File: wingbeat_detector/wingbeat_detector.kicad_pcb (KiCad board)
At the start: 2 copper layers, 36 x 18 mm, 9 parts, among them J1 USB_C_10137062-00021LF, J2 CONN_UMC_JACK_SMD, U1 UAF42_SMA, U2 MAX865EUA+

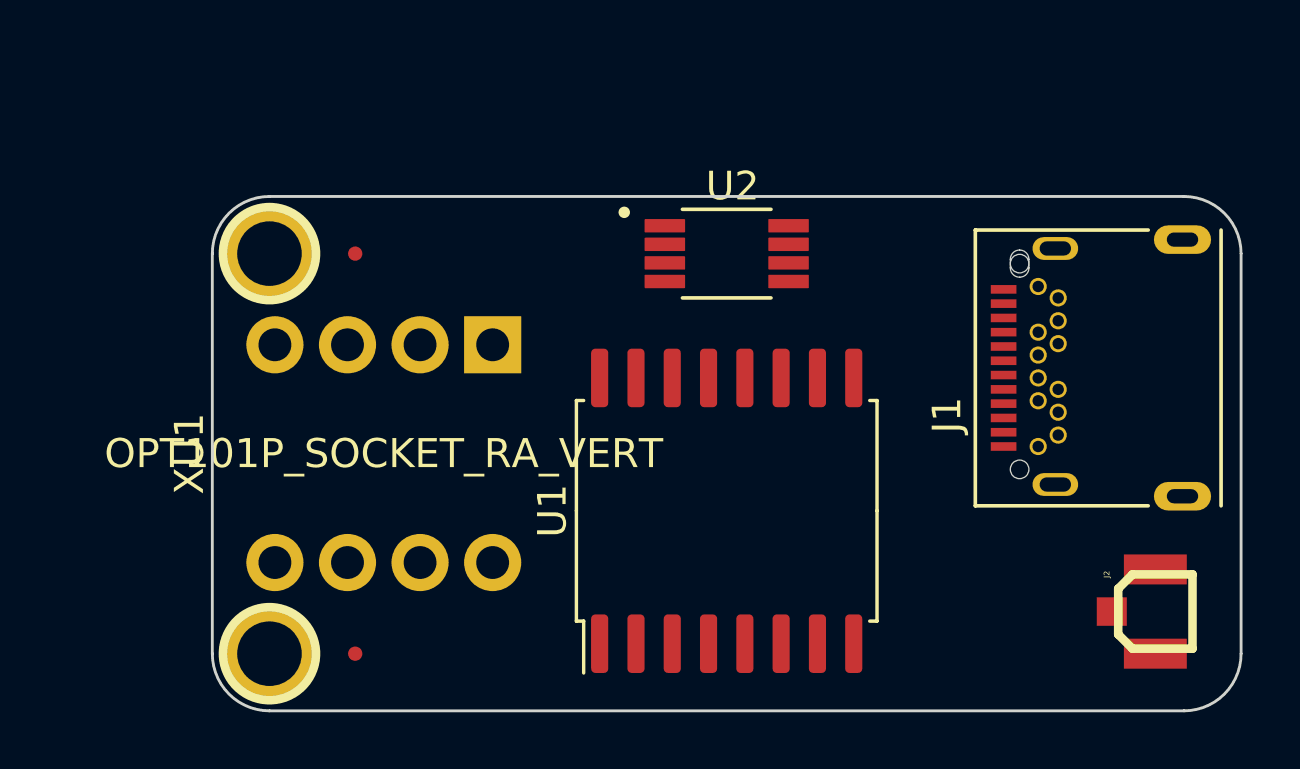
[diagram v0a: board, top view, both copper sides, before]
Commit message: Remove OPT101 and replace
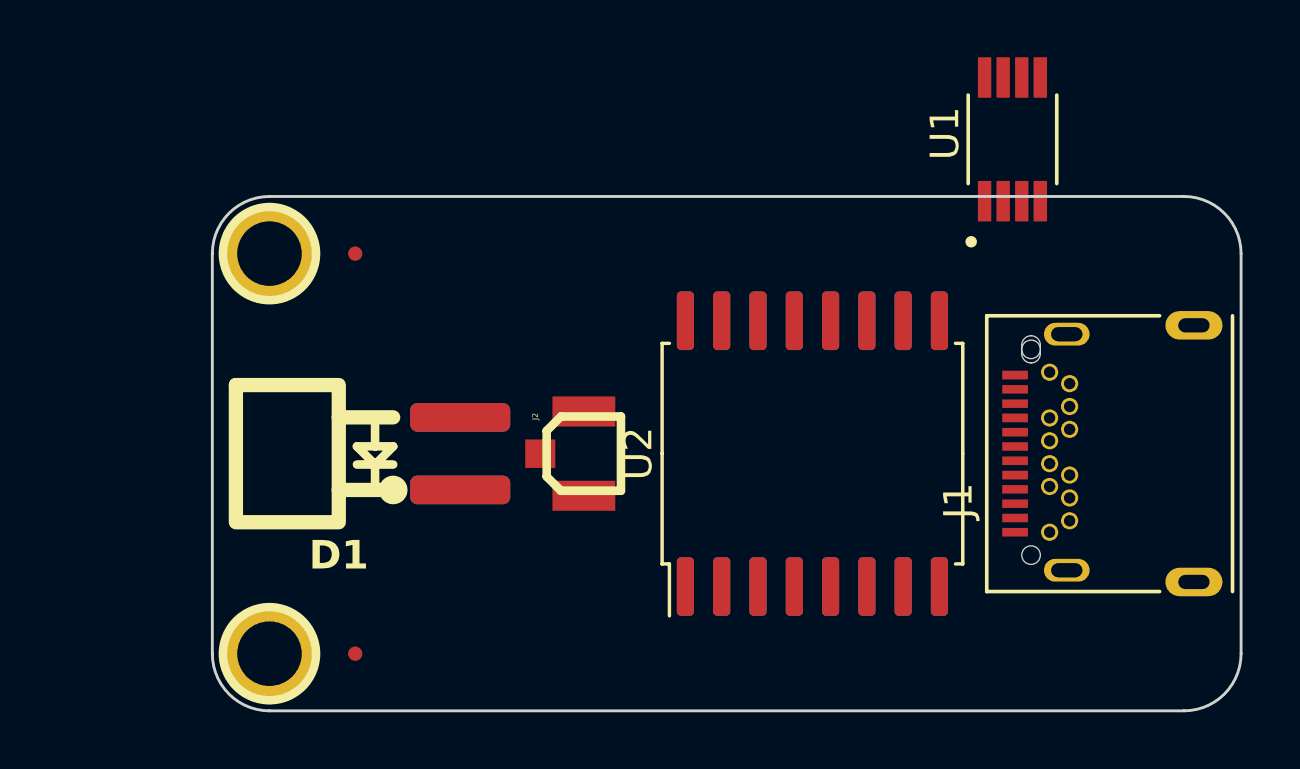
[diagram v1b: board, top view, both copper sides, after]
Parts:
- removed XU1: OPT101P_SOCKET_RA_VERT, Janelia:SOCKET_DIP_2x4_RA_VERT
- added D1: PHOTODIODE, Janelia:PHOTODIODE_RADIAL_RA_SMD_BRIGHT, F.Cu at (136.4, 100.0)
- added D2: LED, Janelia:LED_RADIAL_RA_SMD_BRIGHT, B.Cu at (136.4, 100.0)
- added U3: UAF42_SMA, Janelia:SOIC-16W_7.5x10.3mm_P1.27mm, B.Cu at (153.0, 100.0)
- U1: value UAF42_SMA -> MAX865EUA+; footprint Janelia:SOIC-16W_7.5x10.3mm_P1.27mm -> Janelia:SOP65P490X110-8N
- U2: value MAX865EUA+ -> UAF42_SMA; footprint Janelia:SOP65P490X110-8N -> Janelia:SOIC-16W_7.5x10.3mm_P1.27mm
- moved J2 20.7 mm to (145.0, 100.0)
- moved U1 16.4 mm to (160.0, 89.0)
- moved U2 7.62 mm to (153.0, 100.0), turned to 90 degrees
- moved J1 3.03 mm to (160.7, 100.0)

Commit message: Add sheets
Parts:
- added FID3: FIDUCIAL_0.5mm_MASK1mm, Janelia:FIDUCIAL_0.5mm_Mask1mm, F.Cu at (163.0, 107.0)
- added FID4: FIDUCIAL_0.5mm_MASK1mm, Janelia:FIDUCIAL_0.5mm_Mask1mm, B.Cu at (137.0, 107.0)
- added H3: MOUNTING_HOLE_2, Janelia:MOUNTING_HOLE_2, F.Cu at (166.0, 107.0)
- added H4: MOUNTING_HOLE_2, Janelia:MOUNTING_HOLE_2, F.Cu at (134.0, 107.0)
- added U4: UAF42_SMA, Janelia:SOIC-16W_7.5x10.3mm_P1.27mm, F.Cu at (144.3, 79.6)
- FID2, J2: moved to B.Cu
- U1: value MAX865EUA+ -> OPA818xDRG; footprint Janelia:SOP65P490X110-8N -> Janelia:WSON-8-1EP_3x3mm_P0.5mm_EP1.45x2.4mm
- U2: value UAF42_SMA -> MAX865EUA+; footprint Janelia:SOIC-16W_7.5x10.3mm_P1.27mm -> Janelia:SOP65P490X110-8N
- moved H2 34.9 mm to (166.0, 93.0)
- moved FID2 29.5 mm to (163.0, 93.0), turned to 180 degrees
- moved U2 26.4 mm to (177.0, 89.0)
- moved J2 21.0 mm to (166.0, 100.0), turned to -90 degrees
- moved J1 0.35 mm to (161.0, 100.0)

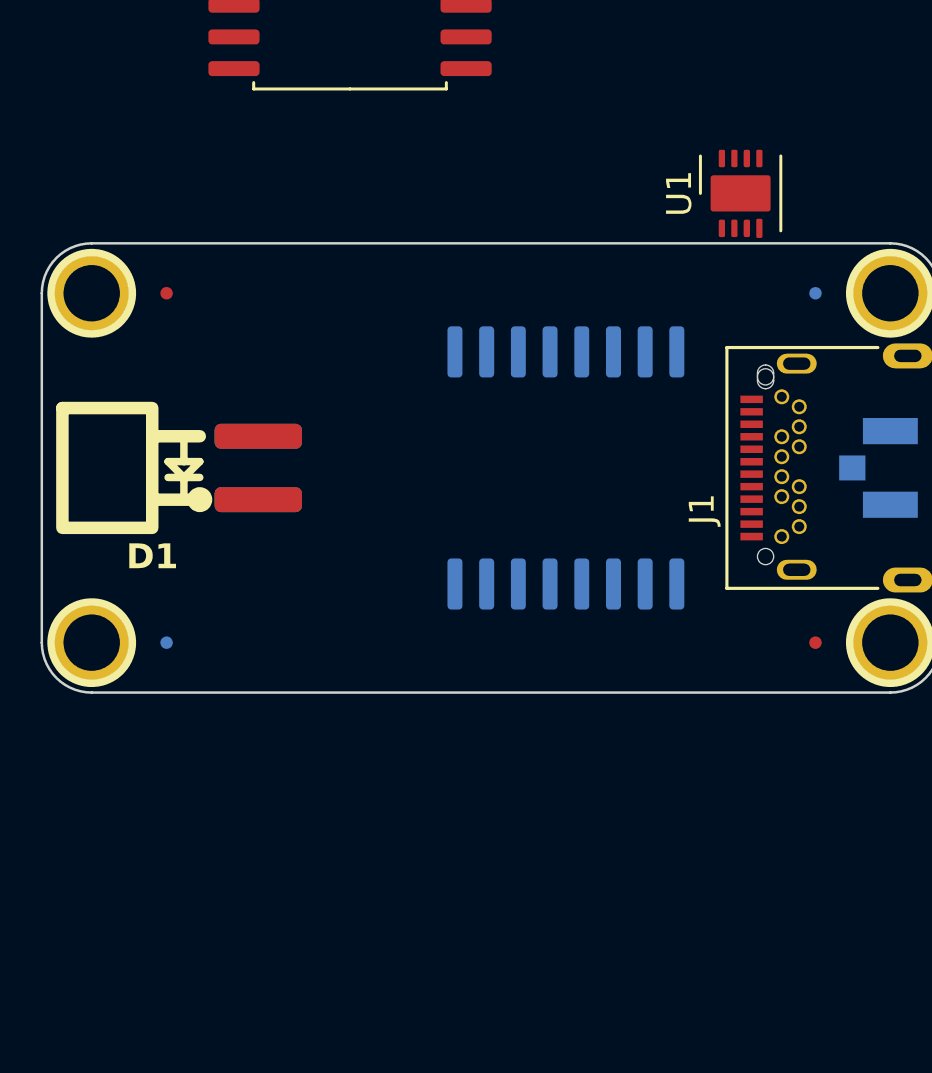
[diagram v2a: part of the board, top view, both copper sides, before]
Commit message: Add led driver
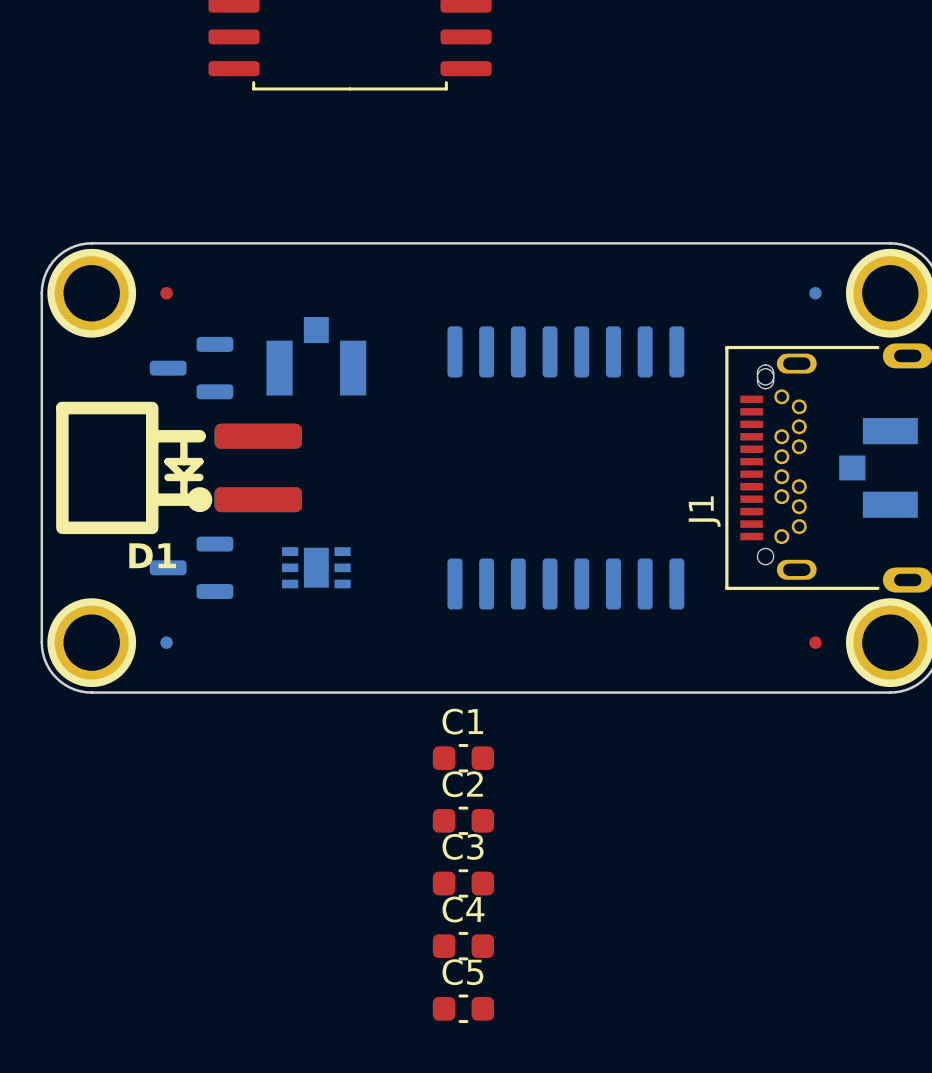
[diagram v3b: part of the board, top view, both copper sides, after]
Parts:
- added C1: 4.7uF, Janelia:C_0603_1608Metric, F.Cu at (148.9, 111.6)
- added C2: 4.7uF, Janelia:C_0603_1608Metric, F.Cu at (148.9, 114.1)
- added C3: 4.7uF, Janelia:C_0603_1608Metric, F.Cu at (148.9, 116.7)
- added C4: 4.7uF, Janelia:C_0603_1608Metric, F.Cu at (148.9, 119.2)
- added C5: 4.7uF, Janelia:C_0603_1608Metric, F.Cu at (148.9, 121.7)
- added J3: CONN_UMC_JACK_SMD, Janelia:UMC_AMPHENOL_A-1JB, B.Cu at (143.0, 96.0)
- added Q1: MOSFET-P-CH, Janelia:SOT-23-3, B.Cu at (138.0, 104.0)
- added Q2: MOSFET-N-CH, Janelia:SOT-23-3, B.Cu at (138.0, 96.0)
- U1: value OPA818xDRG -> LED_DRV_50mA; footprint Janelia:WSON-8-1EP_3x3mm_P0.5mm_EP1.45x2.4mm -> Janelia:DFN-6-1EP_2x2mm_P0.65mm_EP1x1.6mm; moved to B.Cu
- moved U1 22.7 mm to (143.0, 104.0), turned to 180 degrees
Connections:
- D2 pad 1: unconnected-(D2-K-Pad1) -> Net-(D2-K)
- D2 pad 2: unconnected-(D2-A-Pad2) -> Net-(D2-A)
- J1 pad A1: unconnected-(J1-GND-PadA1) -> /GND
- J1 pad A12: unconnected-(J1-GND-PadA12) -> /GND
- J1 pad A4: unconnected-(J1-VBUS_A-PadA4) -> /VA
- J1 pad A9: unconnected-(J1-VBUS_A-PadA9) -> /VA
- J1 pad B1: unconnected-(J1-GND-PadB1) -> /GND
- J1 pad B12: unconnected-(J1-GND-PadB12) -> /GND
- J1 pad B4: unconnected-(J1-VBUS_B-PadB4) -> /VA
- J1 pad B9: unconnected-(J1-VBUS_B-PadB9) -> /VA
- J2 pad 1: unconnected-(J2-In-Pad1) -> /PHOTODIODE_FILTERED
- J2 pad 2: unconnected-(J2-Ext-Pad2) -> /GND
- U1 pad 1: unconnected-(U1-~{PD}-Pad1) -> Net-(D2-A)
- U1 pad 2: unconnected-(U1-FB-Pad2) -> (no net)
- U1 pad 3: unconnected-(U1---Pad3) -> Net-(D2-K)
- U1 pad 5: unconnected-(U1-V--Pad5) -> (no net)
- U2 pad 1: unconnected-(U2-C1--Pad1) -> /power/C1-
- U2 pad 2: unconnected-(U2-C2+-Pad2) -> /power/C2+
- U2 pad 3: unconnected-(U2-C2--Pad3) -> /power/C2-
- U2 pad 4: unconnected-(U2-V--Pad4) -> /VS-
- U2 pad 5: unconnected-(U2-GND-Pad5) -> /GND
- U2 pad 6: unconnected-(U2-IN-Pad6) -> /VUSB
- U2 pad 7: unconnected-(U2-V+-Pad7) -> /VS+
- U2 pad 8: unconnected-(U2-C1+-Pad8) -> /power/C1+

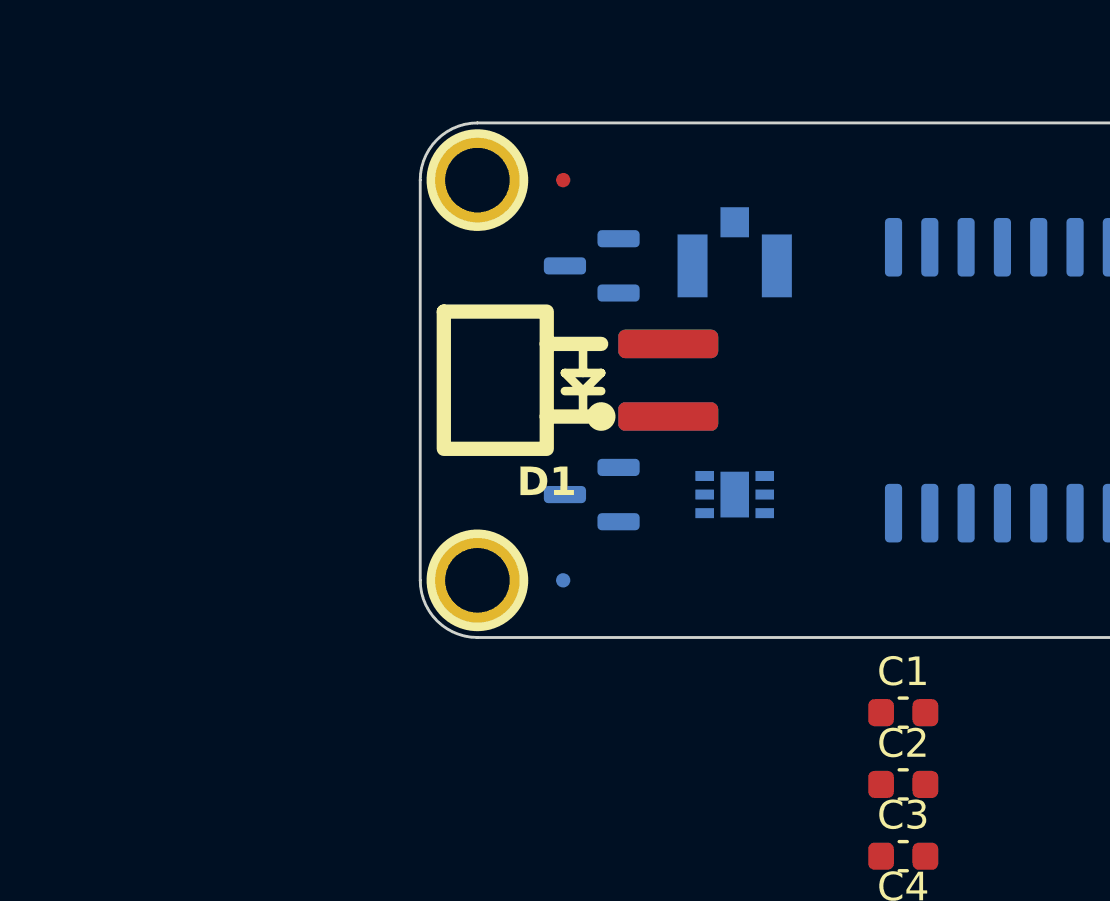
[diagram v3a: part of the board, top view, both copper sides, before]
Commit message: Add mosfet and opa381
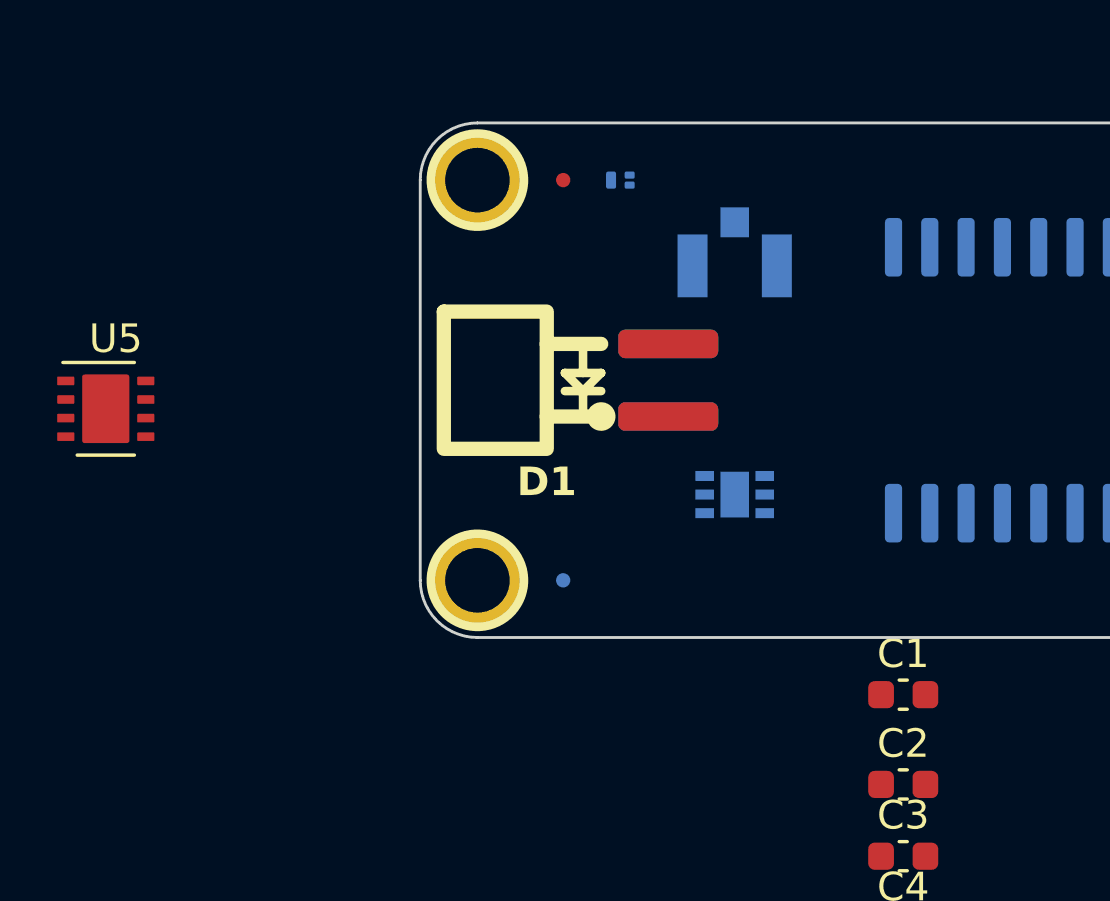
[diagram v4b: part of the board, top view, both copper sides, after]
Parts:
- removed Q2: MOSFET-N-CH, Janelia:SOT-23-3
- added U5: OPA381, Janelia:VSON-8-1EP_3x3mm_P0.65mm_EP1.65x2.4mm, F.Cu at (121.0, 101.0)
- Q1: value MOSFET-P-CH -> MOSFET-N-CH; footprint Janelia:SOT-23-3 -> Janelia:XFDFN-3
- moved Q1 11.0 mm to (139.0, 93.0), turned to 90 degrees
- moved C1 0.63 mm to (148.9, 111.0)
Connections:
- net /VS+ renamed /V10+
- net /VS- renamed /V10-
- C1 pad 1: /VUSB -> /V5+
- J1 pad A4: /VA -> /V5+
- J1 pad A9: /VA -> /V5+
- J1 pad B4: /VA -> /V5+
- J1 pad B9: /VA -> /V5+
- Q1 pad 1: unconnected-(Q1-G-Pad1) -> /LED_ENABLE
- Q1 pad 2: /VA -> /GND
- U1 pad 4: unconnected-(U1-VB-Pad4) -> /led/VB
- U1 pad 6: unconnected-(U1-VA-Pad6) -> /V5+
- U1 pad 7: unconnected-(U1-EP-Pad7) -> /GND
- U2 pad 6: /VUSB -> /V5+
